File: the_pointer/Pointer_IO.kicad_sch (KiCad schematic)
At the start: 25 parts, among them J1 Screw_Terminal_01x06, J4 Screw_Terminal_01x06, J5 R41-B583A, Q1 AS2312, Q2 AS2312, Q3 AS2312, Q4 AS2312, Q5 AS2312, Q6 AS2312, U13 TPD4S014DSQR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

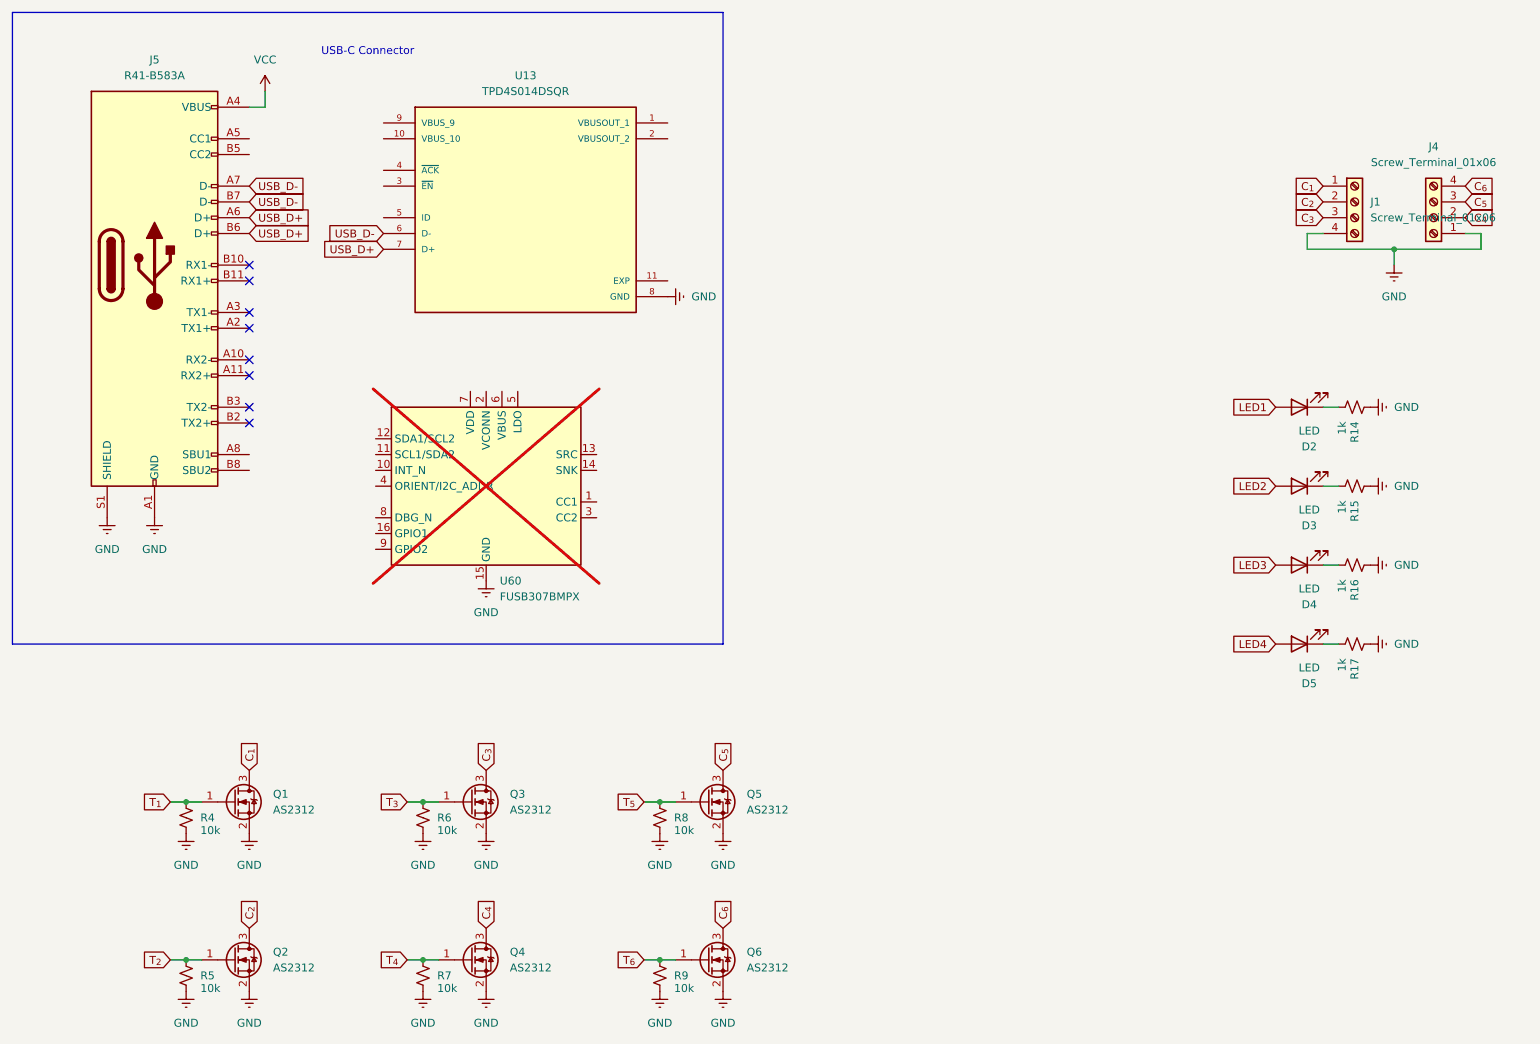
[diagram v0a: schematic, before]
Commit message: Routed Pointer RF transmitter
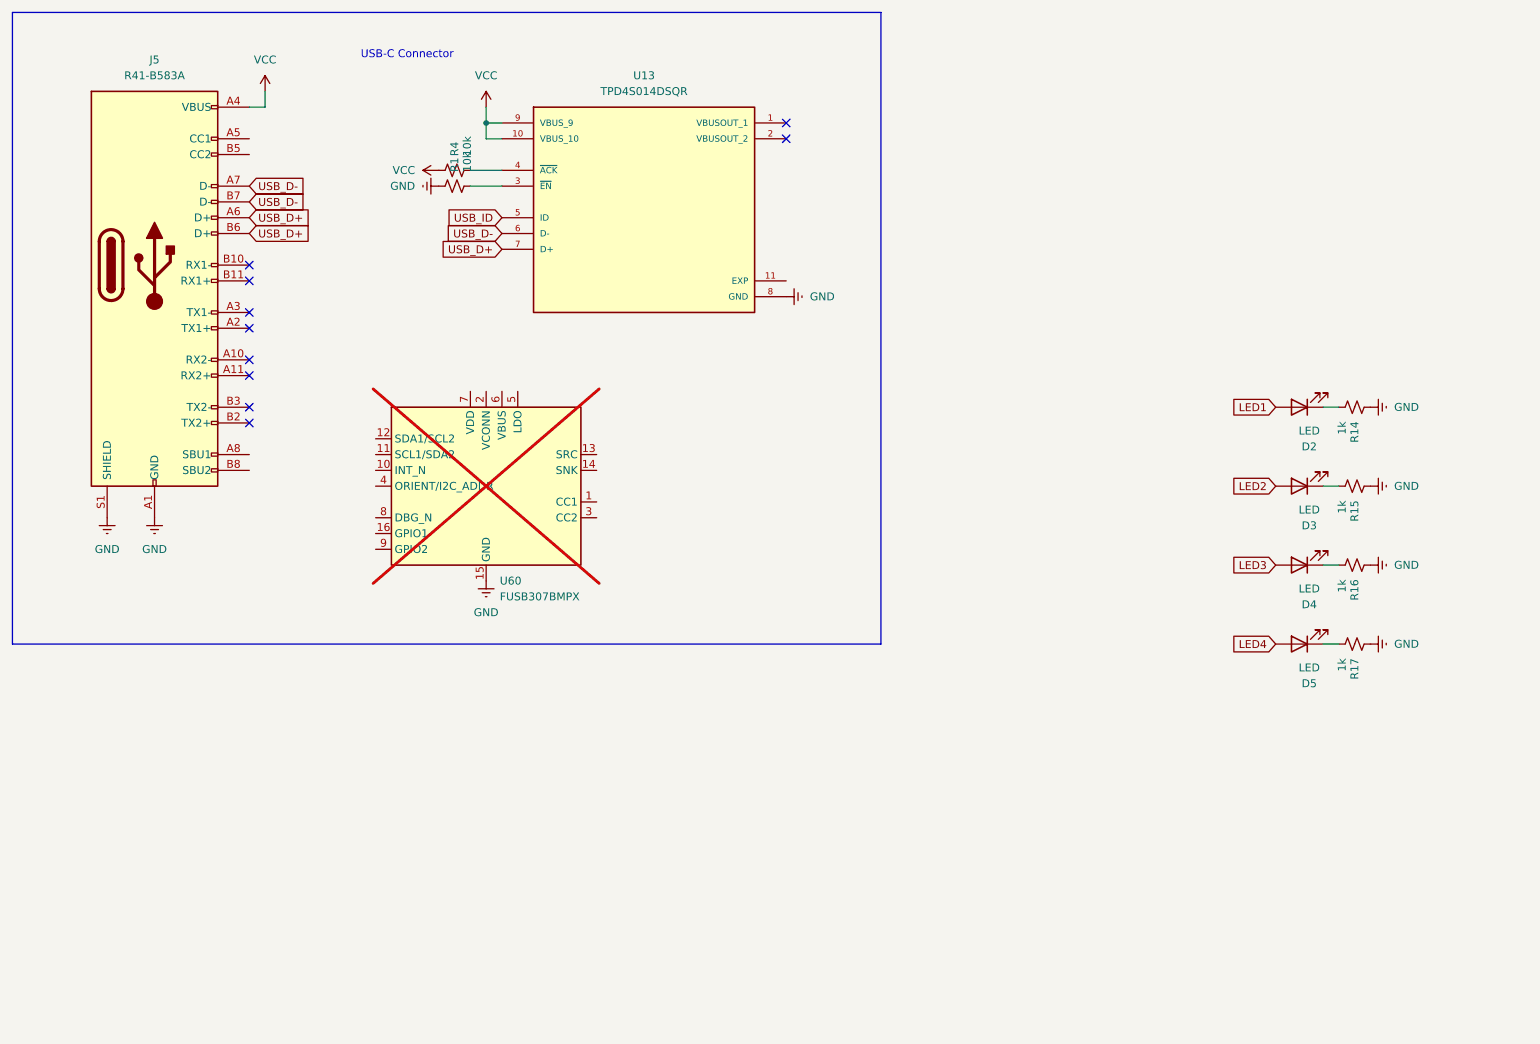
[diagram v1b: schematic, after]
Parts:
- removed J1, J4: Screw_Terminal_01x06, TerminalBlock_Phoenix:TerminalBlock_Phoenix_MPT-0,5-4-2.54_1x04_P2.54mm_Horizontal, symbol Connector:Screw_Terminal_01x04
- removed Q1, Q2, Q3, Q4, Q5, Q6: AS2312, Package_TO_SOT_SMD:SOT-23, symbol Transistor_FET:2N7002
- removed R5, R6, R7, R8, R9: 10k, Resistor_SMD:R_0603_1608Metric, symbol Device:R_Small_US
- added R1: 10k, Resistor_SMD:R_0603_1608Metric, symbol Device:R_Small_US
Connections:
- net T_{1} is gone; now on net VCC: R4.1
- net GND: now also R1.1; no longer R4.2
- net VCC: now also U13.10 (VBUS_10), U13.9 (VBUS_9)
- net at U13.3 (~{EN}): now also R1.2
- net at U13.4 (~{ACK}): now also R4.2
- net USB_ID: now reaches U13.5 (ID)
- no-connect marks 8 -> 10
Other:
- moved on the sheet: U13

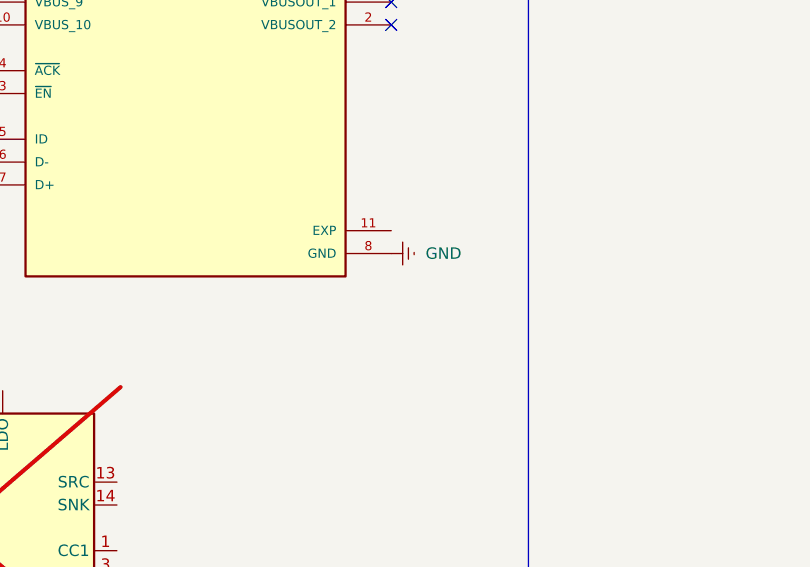
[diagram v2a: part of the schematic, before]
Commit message: Updated Guesser USB and GPS
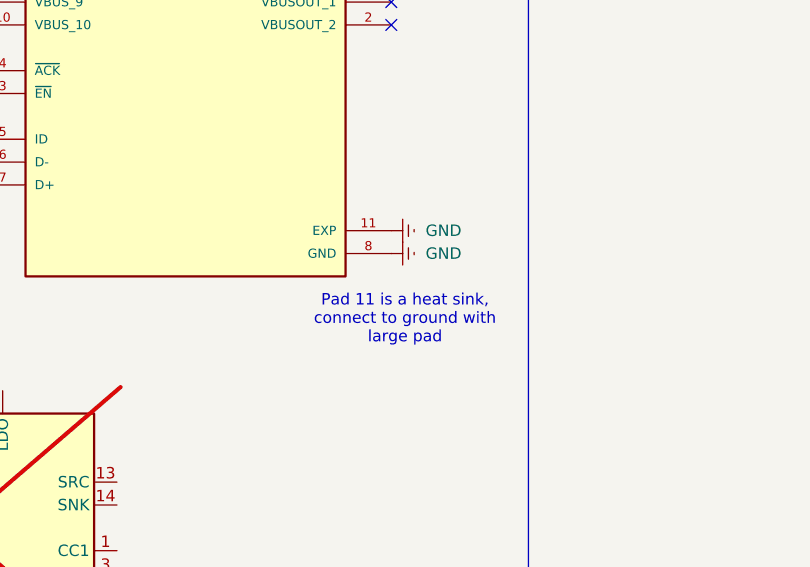
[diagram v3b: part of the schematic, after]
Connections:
- net GND: now also U13.11 (EXP)
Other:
- note added: "Pad 11 is a heat sink, connect to ground with large pad"
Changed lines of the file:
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@@
+		)
+	)
+	(text "Pad 11 is a heat sink, \nconnect to ground with \nlarge pad"
+		(exclude_from_sim no)
+		(at 138.684 65.786 0)
+		(effects
+			(font
+				(size 1.27 1.27)
+			)
 		)
 	)
@@
 					(unit 1)
 				)
+			)
+		)
+	)
+	(symbol
+		(lib_id "power:Earth")
+		(at 137.16 55.88 90)
+		(unit 1)
+		(exclude_from_sim no)
+		(in_bom yes)
+		(on_board yes)
+		(dnp no)
+		(fields_autoplaced yes)
+		(property "Reference" "#PWR052"
+			(at 143.51 55.88 0)
+			(effects
+				(font
+					(size 1.27 1.27)
+				)
+				(hide yes)
+			)
+		)
+		(property "Value" "GND"
+			(at 140.97 55.8799 90)
+			(effects
+				(font
+					(size 1.27 1.27)
+				)
+				(justify right)
+			)
+		)
+		(property "Footprint" ""
+			(at 137.16 55.88 0)
+			(effects
+				(font
+					(size 1.27 1.27)
+				)
+				(hide yes)
+			)
+		)
+		(property "Datasheet" "~"
+			(at 137.16 55.88 0)
+			(effects
+				(font
+					(size 1.27 1.27)
+				)
+				(hide yes)
+			)
+		)
+		(property "Description" "Power symbol creates a global label with name \"Earth\""
+			(at 137.16 55.88 0)
+			(effects
+				(font
+					(size 1.27 1.27)
+				)
+				(hide yes)
+			)
+		)
+		(pin "1"
+		)
+		(instances
+			(project "the_pointer"
+				(path "/473e3a2e-6c5e-4995-af4a-e4bf1449cab0/0bcaec57-f6d5-41f0-b678-342e153337b7"
+					(reference "#PWR052")
+					(unit 1)
+				)
